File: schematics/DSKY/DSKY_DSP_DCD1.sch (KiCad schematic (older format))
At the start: 20 parts, among them U13 74LS02, U15 74LS27, U17 74LS32, U36 74LS00, U41 74LS244, U45 74LS08, U46 74LS04, U47 74LS126, U48 74LS00, U51 74LS244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

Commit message: Add files via upload
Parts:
- removed U36: 74LS00, symbol 74xx:74LS00
- removed unit 2 of U47
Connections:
- net at U17.13, U41.19 (OEb), U48.2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: now also U46.2; no longer U46.8
- net at U60.6: now also U46.1; no longer U46.9
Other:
- note removed: "+5V = Hex\nFloat = Code B"
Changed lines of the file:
@@
 Text Label 4950 5500 0    50   ~ 0
 RWD9
-$Comp
-L 74xx:74LS126 U47
-U 2 1 6755A017
-P 9150 1050
-F 0 "U47" H 9150 1367 50  0000 C CNN
-F 1 "74LS126" H 9150 1276 50  0000 C CNN
-F 2 "" H 9150 1050 50  0001 C CNN
-F 3 "http://www.ti.com/lit/gpn/sn74LS126" H 9150 1050 50  0001 C CNN
-	2    9150 1050
-	1    0    0    -1
-$EndComp
-Text HLabel 9450 1050 2    50   Output ~ 0
-MODE1
-$Comp
-L power:+5V #PWR?
-U 1 1 6755CF6C
-P 8850 1050
-AR Path="/60F98A64/637944C1/6755CF6C" Ref="#PWR?"  Part="1"
-AR Path="/60F98A64/64844A8A/6755CF6C" Ref="#PWR0198"  Part="1"
-F 0 "#PWR0198" H 8850 900 50  0001 C CNN
-F 1 "+5V" H 8865 1223 50  0000 C CNN
-F 2 "" H 8850 1050 50  0001 C CNN
-F 3 "" H 8850 1050 50  0001 C CNN
-	1    8850 1050
-	1    0    0    -1
-$EndComp
-Text Notes 9300 1400 0    80   ~ 0
-+5V = Hex\nFloat = Code B
 Wire Wire Line
 	5300 3500 5300 3600
 Wire Wire Line
-	9150 1300 9150 1600
-Wire Wire Line
 	5300 3600 6500 3600
 Wire Wire Line
 	5250 1300 5250 1800
-Wire Wire Line
-	8550 1500 8400 1500
-Wire Wire Line
-	8550 1700 8500 1700
 Entry Wire Line
 	7700 5500 7800 5600
@@
 $Comp
 L 74xx:74LS04 U46
-U 4 1 67B76243
+U 1 1 67B76243
 P 1800 3750
 F 0 "U46" H 1800 4067 50  0000 C CNN
@@
 F 2 "" H 1800 3750 50  0001 C CNN
 F 3 "http://www.ti.com/lit/gpn/sn74LS04" H 1800 3750 50  0001 C CNN
-	4    1800 3750
+	1    1800 3750
 	1    0    0    -1
 $EndComp
@@
 F 3 "http://www.ti.com/lit/gpn/sn74ls02" H 5800 5000 50  0001 C CNN
 	4    5800 5000
-	1    0    0    -1
-$EndComp
-$Comp
-L 74xx:74LS00 U36
-U 3 1 67DD8A24
-P 8850 1600
-F 0 "U36" H 8850 1925 50  0000 C CNN
-F 1 "74LS00" H 8850 1834 50  0000 C CNN
-F 2 "" H 8850 1600 50  0001 C CNN
-F 3 "http://www.ti.com/lit/gpn/sn74ls00" H 8850 1600 50  0001 C CNN
-	3    8850 1600
 	1    0    0    -1
 $EndComp
@@
 Wire Wire Line
 	8500 3150 9150 3150
-Connection ~ 8400 3250
 Wire Wire Line
 	8400 3250 8400 3600
 Wire Wire Line
-	8400 1500 8400 3250
-Connection ~ 8500 3150
-Wire Wire Line
-	8500 3150 8500 1700
-Wire Wire Line
 	9050 2950 9150 2950

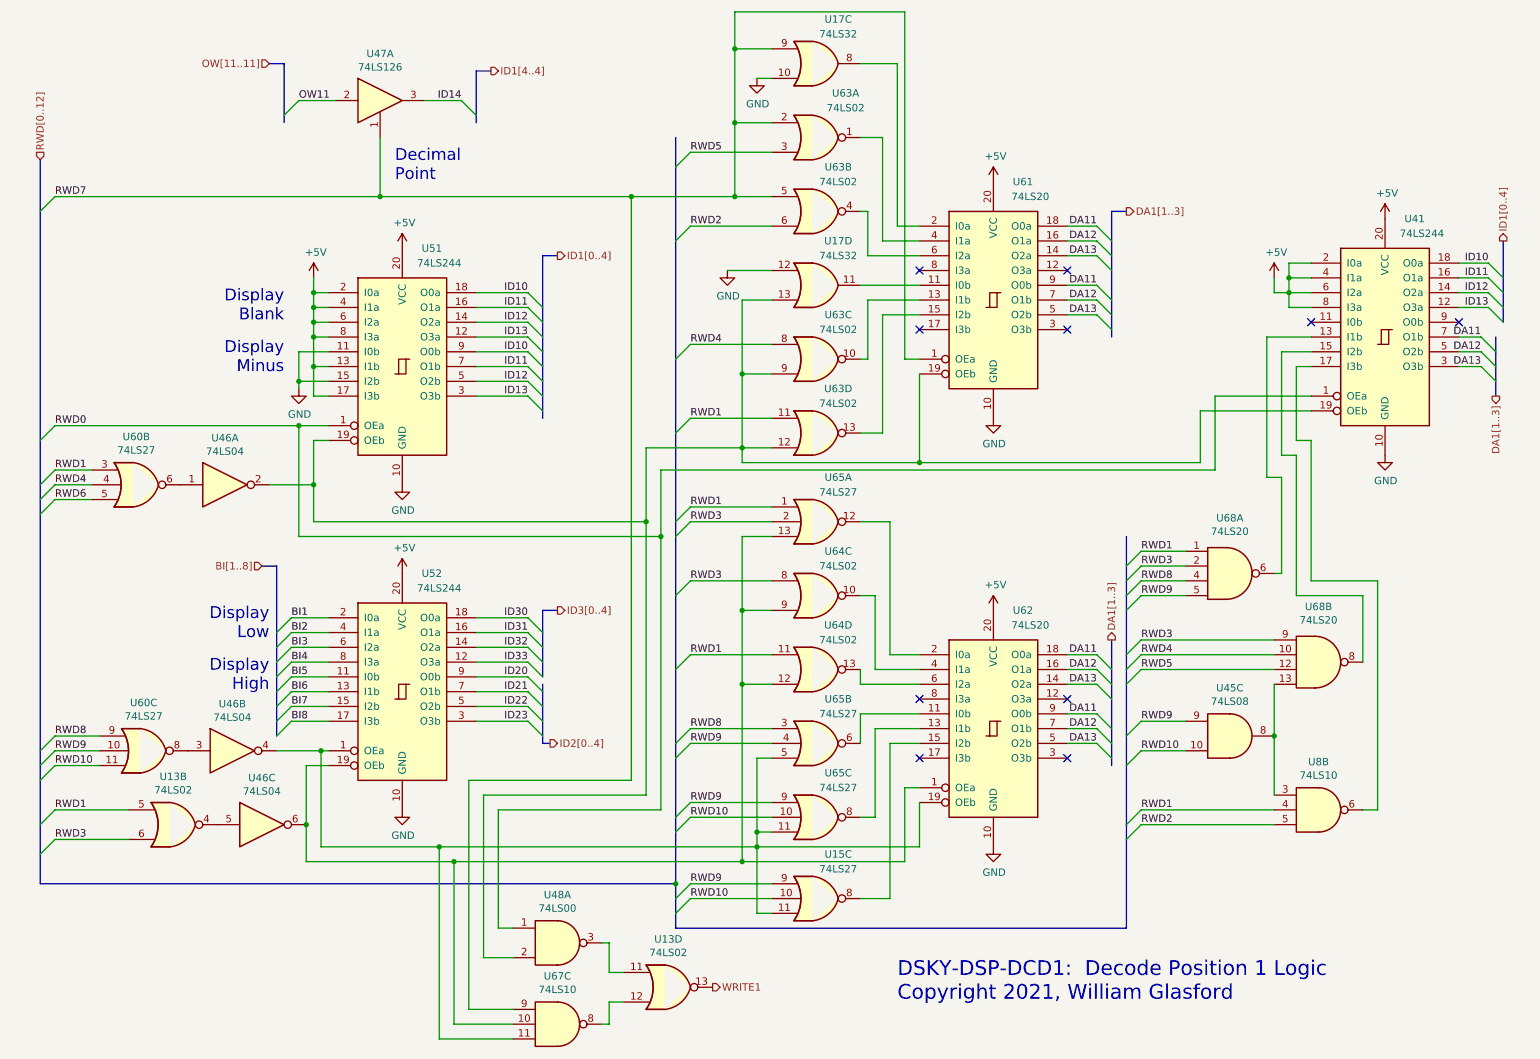
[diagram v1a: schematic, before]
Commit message: Minor tweaks to the display decoding logic.
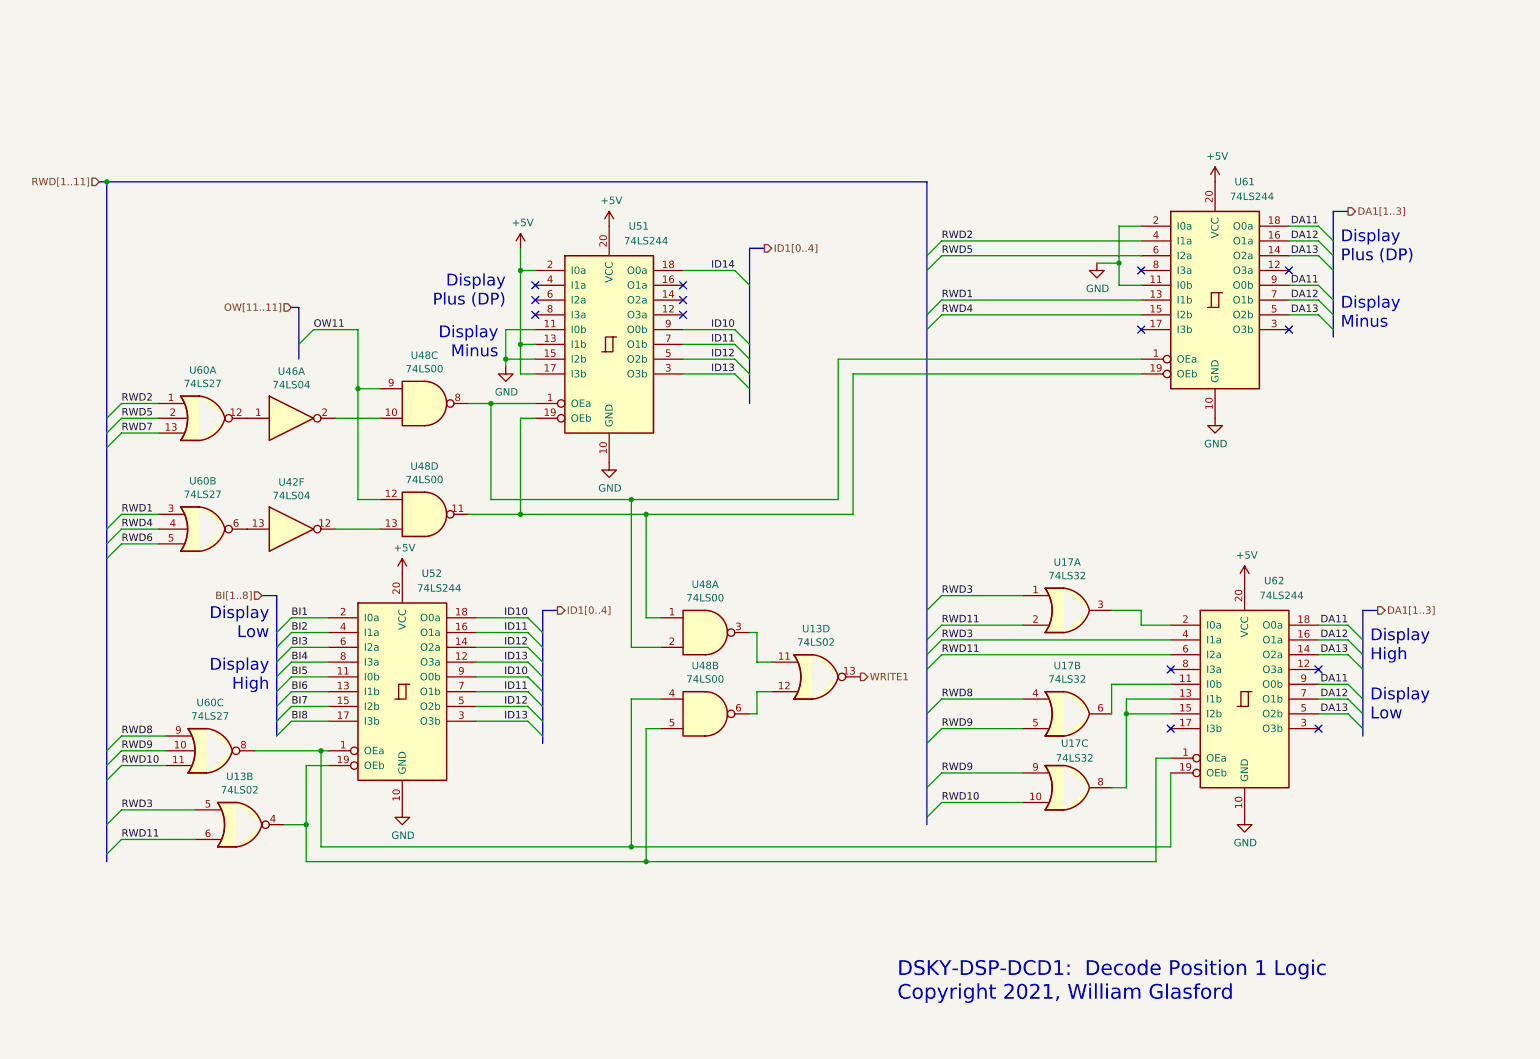
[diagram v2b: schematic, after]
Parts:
- removed U15, U65: 74LS27, symbol 74xx:74LS27
- removed unit 4 of U17
- removed U41: 74LS244, symbol 74xx:74LS244
- removed U45: 74LS08, symbol 74xx:74LS08
- removed unit 3 of U46
- removed unit 2 of U46
- removed U47: 74LS126, symbol 74xx:74LS126
- removed U63, U64: 74LS02, symbol 74xx:74LS02
- removed U67, U8: 74LS10, symbol 74xx:74LS10
- removed U68: 74LS20, symbol 74xx:74LS20
- added unit 1 of U17
- added unit 2 of U17
- added U42: 74LS04, symbol 74xx:74LS04
- added unit 2 of U48
- added unit 4 of U48
- added unit 3 of U48
- added unit 1 of U60
- U61, U62: value 74LS20 -> 74LS244
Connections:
- net ID20 is gone; now on net ID10: U52.9 (O0b)
- net ID21 is gone; now on net ID11: U52.7 (O1b)
- net ID22 is gone; now on net ID12: U52.5 (O2b)
- net ID23 is gone; now on net ID13: U52.3 (O3b)
- net ID30 is gone; now on net ID10: U52.18 (O0a)
- net ID31 is gone; now on net ID11: U52.16 (O1a)
- net ID32 is gone; now on net ID12: U52.14 (O2a)
- net ID33 is gone; now on net ID13: U52.12 (O3a)
- net +5V: no longer U51.4 (I1a), U51.6 (I2a), U51.8 (I3a)
- net GND: now also U61.11 (I0b), U61.2 (I0a); no longer U17.10
- net ID10: no longer U51.18 (O0a)
- net ID11: no longer U51.16 (O1a)
- net ID12: no longer U51.14 (O2a)
- net ID13: no longer U51.12 (O3a)
- net ID14: now also U51.18 (O0a)
- net OW11: now also U48.12, U48.9
- net RWD1: now also U61.13 (I1b); no longer U13.5
- net RWD10: now also U17.10
- net RWD2: now also U61.4 (I1a), U60.1
- net RWD3: now also U13.5, U62.4 (I1a), U17.1; no longer U13.6
- net RWD4: now also U61.15 (I2b)
- net RWD5: now also U61.6 (I2a), U60.2
- net RWD7: now also U60.13; no longer U17.9, U61.1 (OEa)
- net RWD8: now also U17.4
- net RWD9: now also U17.9, U17.5
- net at U51.19 (OEb), U61.19 (OEb): now also U48.1, U48.11; no longer U46.2, U48.2
- net at U52.1 (OEa), U62.19 (OEb): now also U60.8, U48.4
- net at U52.19 (OEb), U62.1 (OEa): now also U13.4, U48.5
- net at U46.1: now also U60.12; no longer U60.6
- net at U17.8: now also U62.13 (I1b), U62.15 (I2b); no longer U61.2 (I0a)
- net at U62.2 (I0a): now also U17.3
- net at U62.11 (I0b): now also U17.6
- net RWD11: now reaches U62.6 (I2a)
- net RWD11: now also U13.6, U17.2
- net at U13.12: now also U48.6
- net RWD0: no longer names the net of U51.1 (OEa)
- net RWD0: now also U48.2, U61.1 (OEa), U48.8; no longer U48.1
- new net: U42.12, U48.13
- new net: U42.13, U60.6
- new net: U46.2, U48.10
- no-connect marks 10 -> 14
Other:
- note added: "Display\nPlus (DP)"
- note removed: "Decimal\nPoint"
- note removed: "Display\nBlank"
- moved on the sheet: U13B, U13D, U48A, U51, U60B, U60C, U61, U62

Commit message: Simplified...
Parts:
- removed unit 4 of U13
- added unit 4 of U17
- added U43: 74LS00, symbol 74xx:74LS00
- renumbered U46 to U42
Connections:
- net WRITE1: now also U43.8
- net at U48.6: now also U17.13
- net at U60.12: now also U42.3; no longer U42.1
- net at U48.10: now also U42.4; no longer U42.2
- net at U48.3: now also U17.12
- net BI1 renamed ID30
- net BI2 renamed ID31
- net BI3 renamed ID32
- net BI4 renamed ID33
- net BI5 renamed ID20
- net BI6 renamed ID21
- net BI7 renamed ID22
- net BI8 renamed ID23
- new net: U17.11, U43.9
- new net CLK2: U43.10

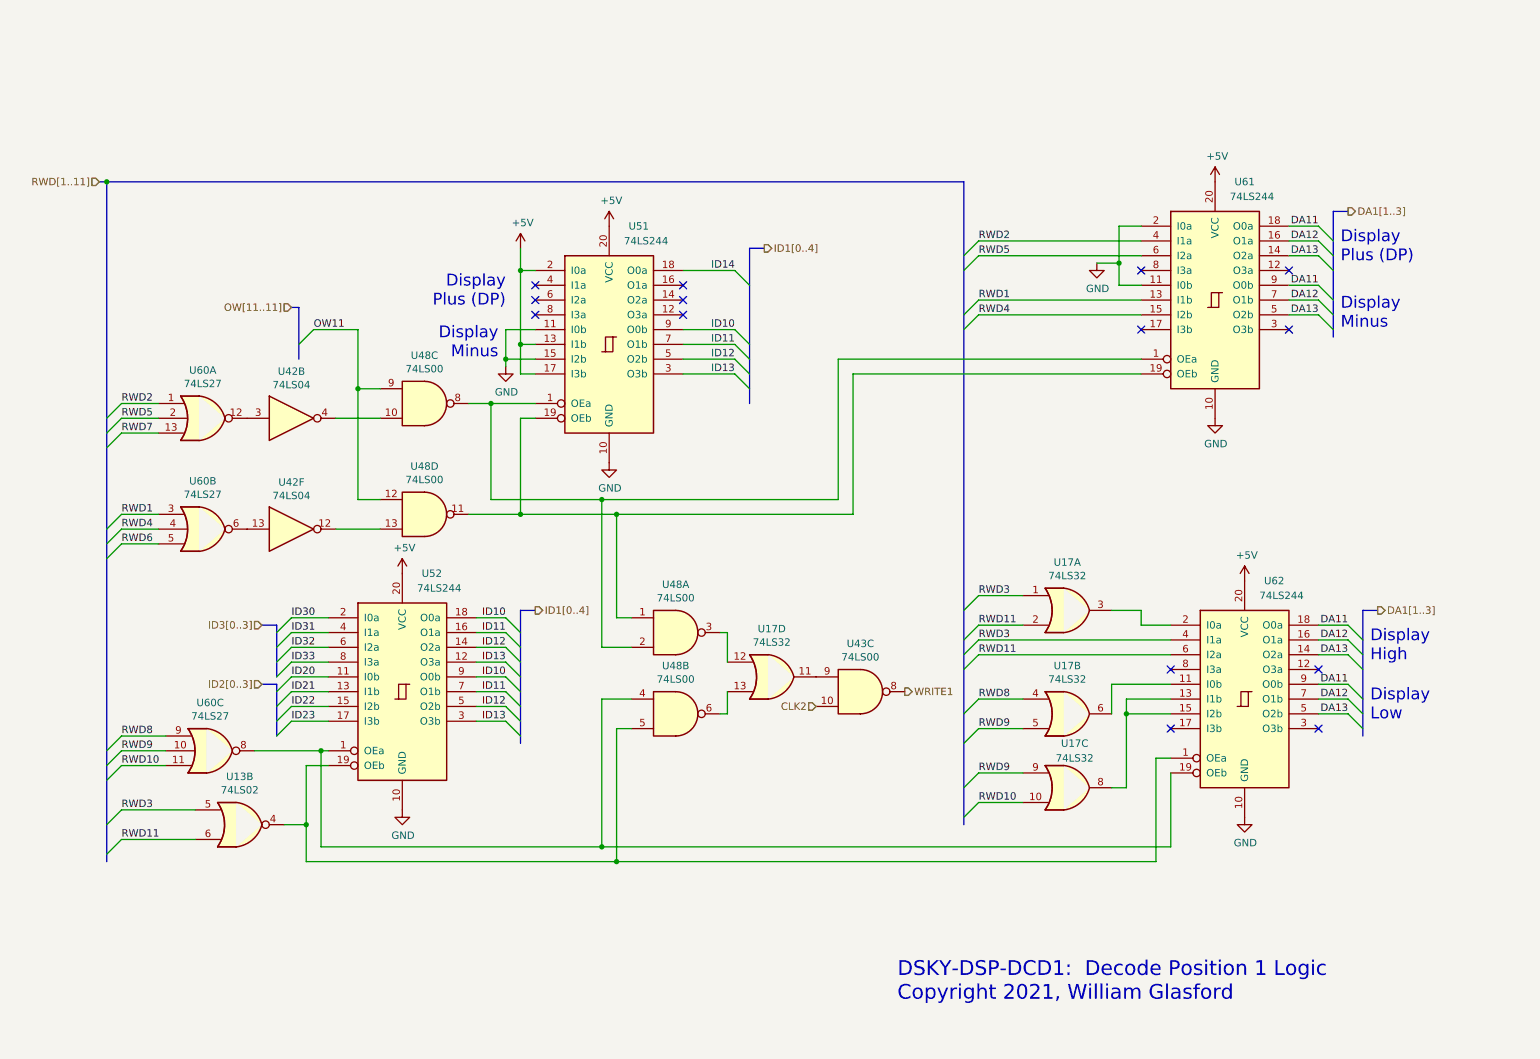
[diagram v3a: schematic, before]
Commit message: Cleaned up clock logic.
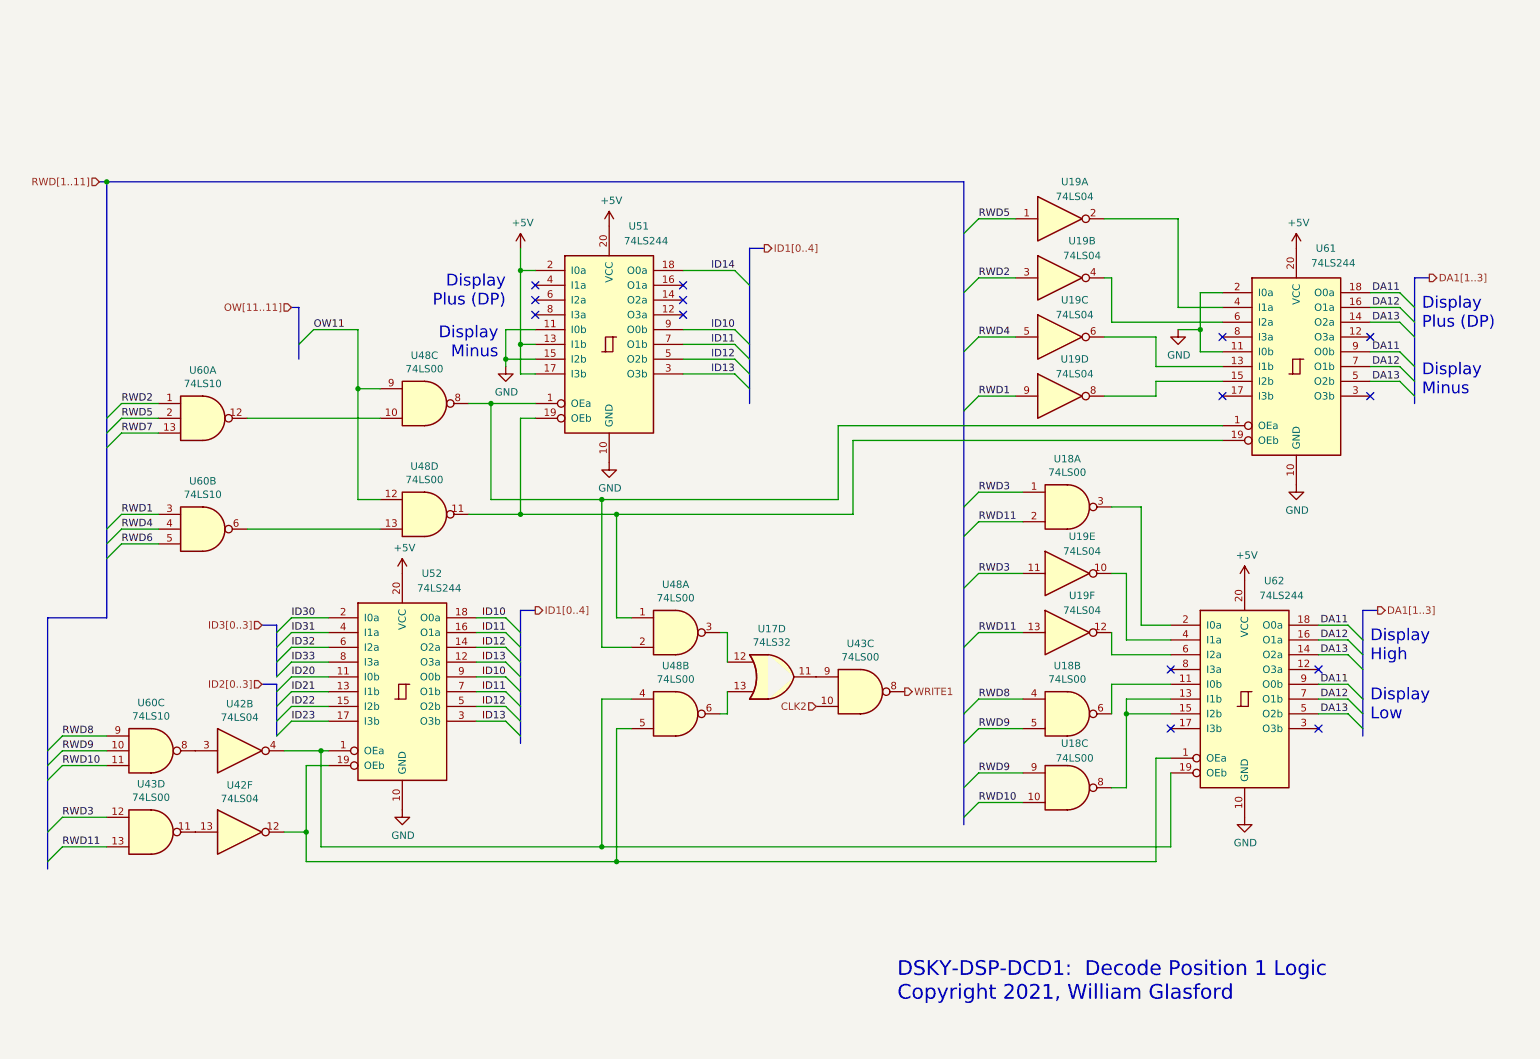
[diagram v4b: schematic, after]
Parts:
- removed U13: 74LS02, symbol 74xx:74LS02
- removed unit 1 of U17
- removed unit 2 of U17
- removed unit 3 of U17
- removed U60: 74LS27, symbol 74xx:74LS27
- added U18: 74LS00, symbol 74xx:74LS00
- added U19: 74LS04, symbol 74xx:74LS04
- added unit 4 of U43
- added U60: 74LS10, symbol 74xx:74LS10
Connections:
- net RWD1: now also U19.9, U60.3; no longer U61.13 (I1b)
- net RWD10: now also U18.10, U60.11
- net RWD11: now also U18.2, U19.13, U43.13; no longer U62.6 (I2a)
- net RWD2: now also U19.3, U60.1; no longer U61.4 (I1a)
- net RWD3: now also U18.1, U19.11, U43.12; no longer U62.4 (I1a)
- net RWD4: now also U19.5, U60.4; no longer U61.15 (I2b)
- net RWD5: now also U19.1, U60.2; no longer U61.6 (I2a)
- net RWD6: now also U60.5
- net RWD7: now also U60.13
- net RWD8: now also U18.4, U60.9
- net RWD9: now also U18.5, U18.9, U60.10
- net at U42.3: now also U60.8
- net at U62.2 (I0a): now also U18.3
- net at U62.11 (I0b): now also U18.6
- net at U62.13 (I1b), U62.15 (I2b): now also U18.8
- net at U48.13: now also U60.6; no longer U42.12
- net at U42.13: now also U43.11
- net at U48.10: now also U60.12; no longer U42.4
- net at U48.4, U52.1 (OEa), U62.19 (OEb): now also U42.4
- net at U48.5, U52.19 (OEb), U62.1 (OEa): now also U42.12
- new net: U19.2, U61.4 (I1a)
- new net: U19.4, U61.6 (I2a)
- new net: U19.6, U61.13 (I1b)
- new net: U19.8, U61.15 (I2b)
- new net: U19.10, U62.4 (I1a)
- new net: U19.12, U62.6 (I2a)
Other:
- moved on the sheet: U42B, U42F, U61
